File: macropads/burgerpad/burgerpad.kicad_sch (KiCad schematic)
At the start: 1 part, among them U1 RP2040-ZERO

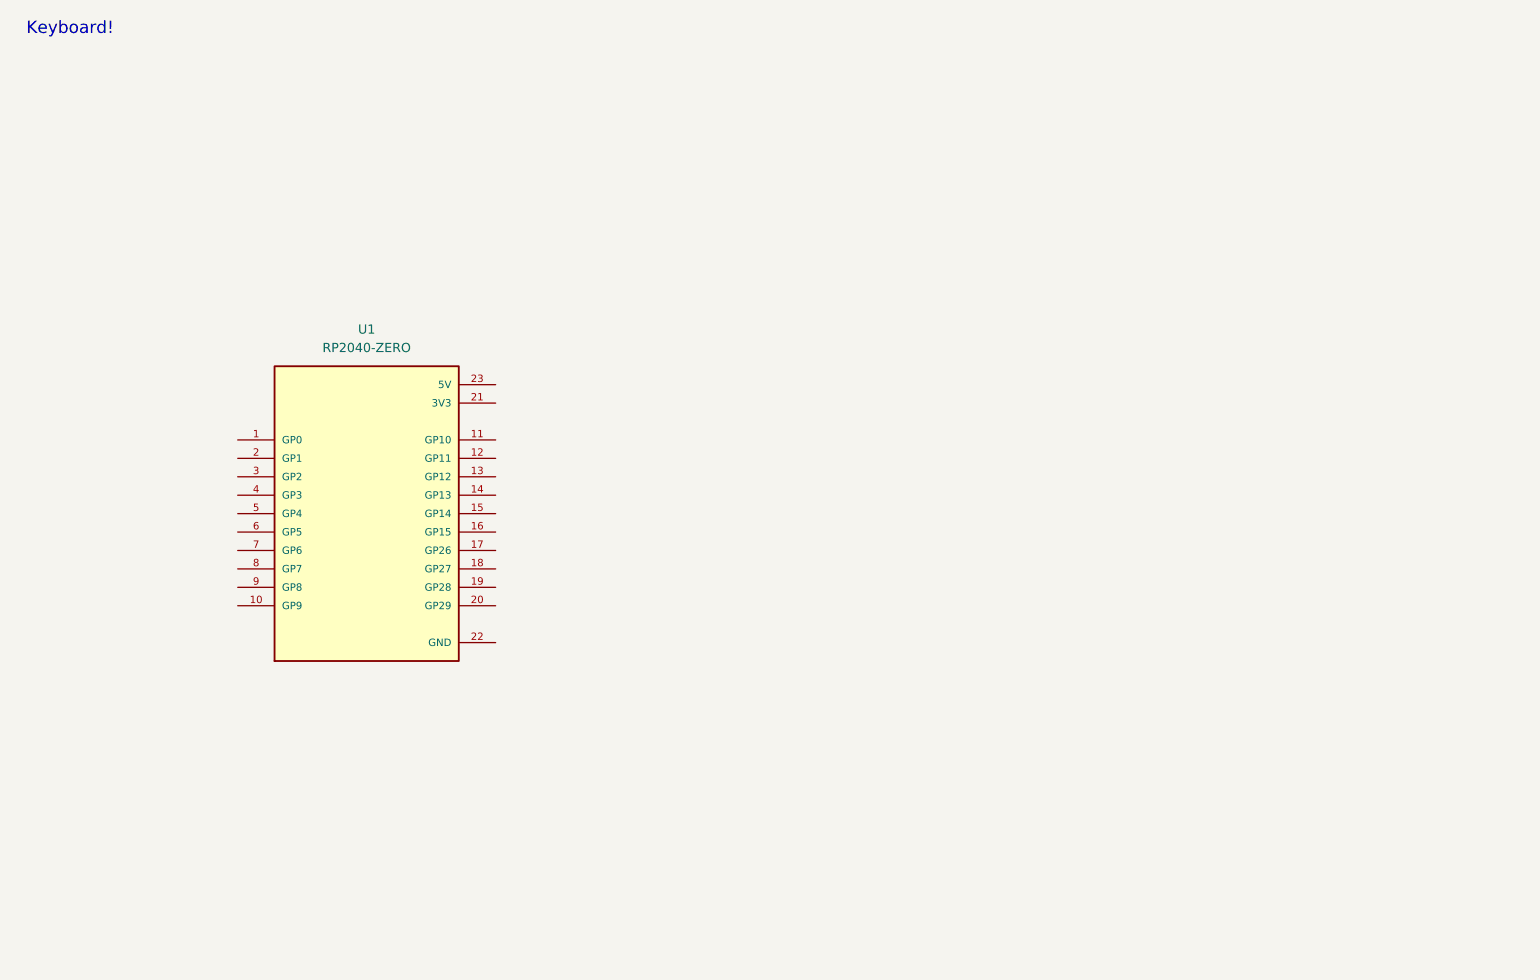
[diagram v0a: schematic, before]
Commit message: Made schematic and did PCB layouts
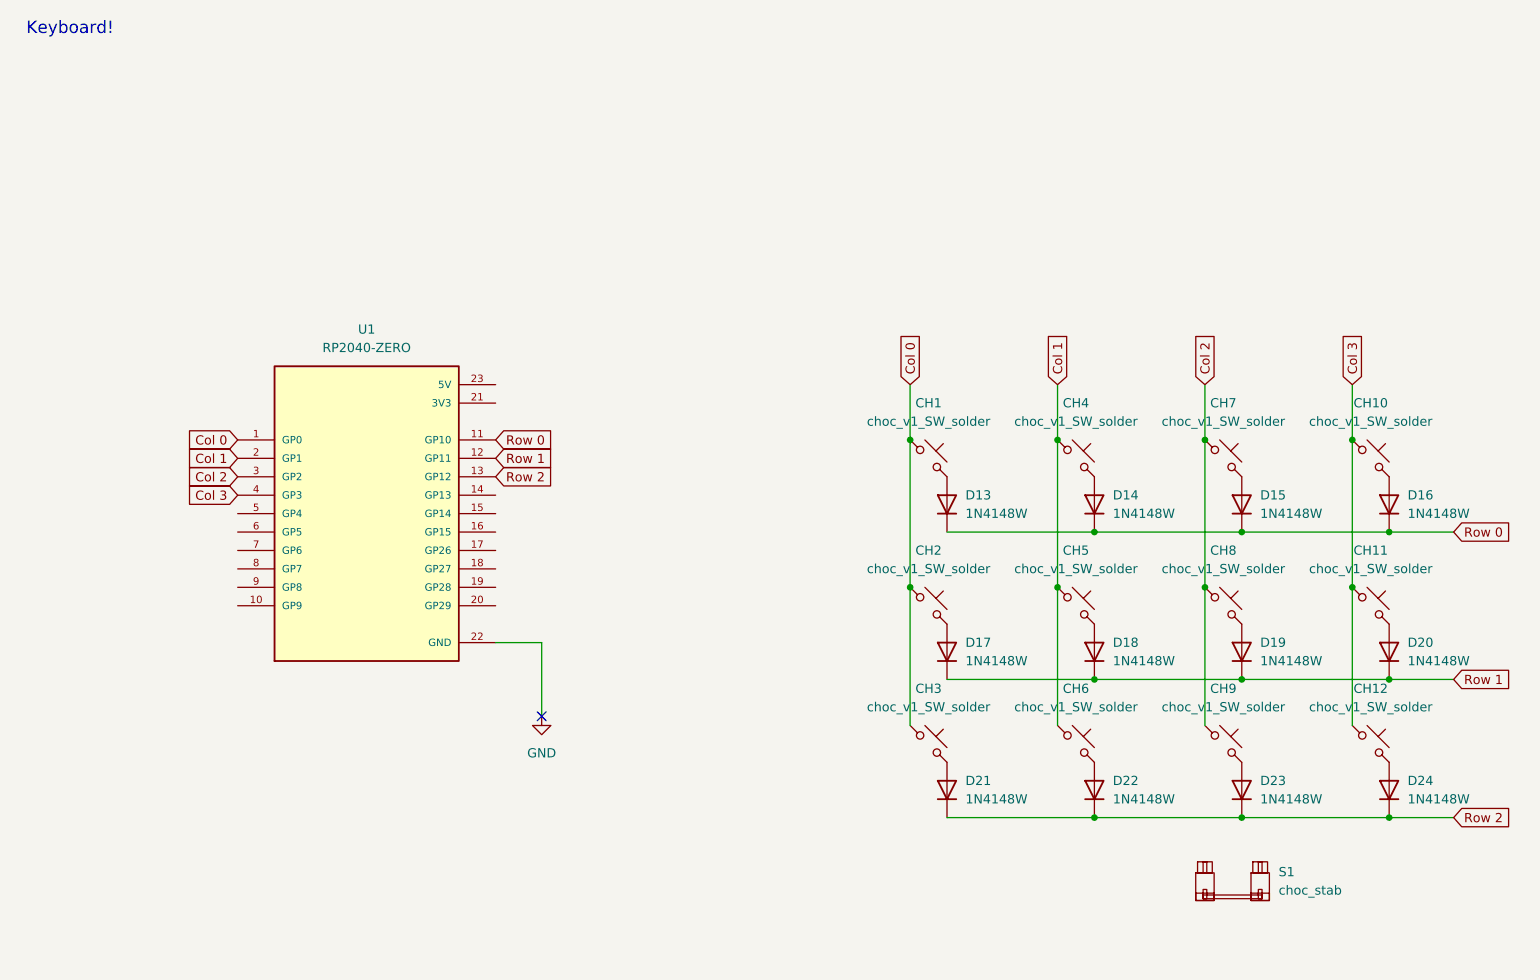
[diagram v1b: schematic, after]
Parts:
- added CH1, CH10, CH11, CH12, CH2, CH3, CH4, CH5, CH6, CH7, CH8, CH9: choc_v1_SW_solder, PCM_marbastlib-choc:SW_choc_v1_1u, symbol PCM_marbastlib-choc:choc_v1_SW_solder
- added D13, D14, D15, D16, D17, D18, D19, D20, D21, D22, D23, D24: 1N4148W, Diode_SMD:D_SOD-123, symbol Diode:1N4148W
- added S1: choc_stab, PCM_marbastlib-xp-choc:STAB_choc_2u, symbol PCM_marbastlib-choc:choc_stab
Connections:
- net Col 0: now reaches U1.1 (GP0)
- net Col 0: now also CH1.1, CH2.1, CH3.1
- net Row 0: now reaches U1.11 (GP10)
- net Row 0: now also D13.1 (K), D14.1 (K), D15.1 (K), D16.1 (K)
- net Row 1: now reaches U1.12 (GP11)
- net Row 1: now also D17.1 (K), D18.1 (K), D19.1 (K), D20.1 (K)
- net Row 2: now reaches U1.13 (GP12)
- net Row 2: now also D21.1 (K), D22.1 (K), D23.1 (K), D24.1 (K)
- net Col 1: now reaches U1.2 (GP1)
- net Col 1: now also CH4.1, CH5.1, CH6.1
- net GND: now reaches U1.22 (GND)
- net Col 2: now reaches U1.3 (GP2)
- net Col 2: now also CH7.1, CH8.1, CH9.1
- net Col 3: now reaches U1.4 (GP3)
- net Col 3: now also CH10.1, CH11.1, CH12.1
- new net: CH4.2, D14.2 (A)
- new net: CH12.2, D24.2 (A)
- new net: CH6.2, D22.2 (A)
- new net: CH1.2, D13.2 (A)
- new net: CH7.2, D15.2 (A)
- new net: CH11.2, D20.2 (A)
- new net: CH10.2, D16.2 (A)
- new net: CH8.2, D19.2 (A)
- new net: CH3.2, D21.2 (A)
- new net: CH5.2, D18.2 (A)
- new net: CH2.2, D17.2 (A)
- new net: CH9.2, D23.2 (A)
- no-connect marks 0 -> 1

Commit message: Updated schematic and PCB to match new layout
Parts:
- removed S1: choc_stab, PCM_marbastlib-xp-choc:STAB_choc_2u, symbol PCM_marbastlib-choc:choc_stab
- added CH13: choc_v1_SW_solder, PCM_marbastlib-choc:SW_choc_v1_1u, symbol PCM_marbastlib-choc:choc_v1_SW_solder
- added D25: 1N4148W, Diode_SMD:D_SOD-123, symbol Diode:1N4148W
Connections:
- net Col 3: now also CH13.1
- net Row 3: now reaches U1.14 (GP13)
- net Row 3: now also D25.1 (K)
- new net: CH13.2, D25.2 (A)
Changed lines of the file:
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@@
 	)
 	(junction
+		(at 199.39 111.76)
+		(diameter 0)
+		(color 0 0 0 0)
+	)
+	(junction
 		(at 158.75 72.39)
 		(diameter 0)
@@
 	(wire
 		(pts
+			(xy 199.39 111.76) (xy 199.39 130.81)
+		)
+		(stroke
+			(width 0)
+			(type default)
+		)
+	)
+	(wire
+		(pts
 			(xy 199.39 64.77) (xy 199.39 72.39)
 		)
@@
 	(wire
 		(pts
+			(xy 204.47 143.51) (xy 213.36 143.51)
+		)
+		(stroke
+			(width 0)
+			(type default)
+		)
+	)
+	(wire
+		(pts
 			(xy 143.51 105.41) (xy 163.83 105.41)
 		)
@@
 		)
 	)
+	(global_label "Row 3"
+		(shape input)
+		(at 81.28 80.01 0)
+		(fields_autoplaced yes)
+		(effects
+			(font
+				(size 1.27 1.27)
+			)
+			(justify left)
+		)
+		(property "Intersheetrefs" "${INTERSHEET_REFS}"
+			(at 90.1918 80.01 0)
+			(hide yes)
+			(show_name no)
+			(do_not_autoplace no)
+			(effects
+				(font
+					(size 1.27 1.27)
+				)
+				(justify left)
+			)
+		)
+	)
 	(global_label "Col 1"
 		(shape input)
@@
 		)
 	)
+	(global_label "Row 3"
+		(shape input)
+		(at 213.36 143.51 0)
+		(fields_autoplaced yes)
+		(effects
+			(font
+				(size 1.27 1.27)
+			)
+			(justify left)
+		)
+		(property "Intersheetrefs" "${INTERSHEET_REFS}"
+			(at 222.2718 143.51 0)
+			(hide yes)
+			(show_name no)
+			(do_not_autoplace no)
+			(effects
+				(font
+					(size 1.27 1.27)
+				)
+				(justify left)
+			)
+		)
+	)
 	(global_label "Row 0"
 		(shape input)
@@
 	(symbol
 		(lib_id "Diode:1N4148W")
+		(at 204.47 139.7 90)
+		(unit 1)
+		(body_style 1)
+		(exclude_from_sim no)
+		(in_bom yes)
+		(on_board yes)
+		(in_pos_files yes)
+		(dnp no)
+		(fields_autoplaced yes)
+		(property "Reference" "D25"
+			(at 207.01 138.4299 90)
+			(show_name no)
+			(do_not_autoplace no)
+			(effects
+				(font
+					(size 1.27 1.27)
+				)
+				(justify right)
+			)
+		)
+		(property "Value" "1N4148W"
+			(at 207.01 140.9699 90)
+			(show_name no)
+			(do_not_autoplace no)
+			(effects
+				(font
+					(size 1.27 1.27)
+				)
+				(justify right)
+			)
+		)
+		(property "Footprint" "Diode_SMD:D_SOD-123"
+			(at 208.915 139.7 0)
+			(hide yes)
+			(show_name no)
+			(do_not_autoplace no)
+			(effects
+				(font
+					(size 1.27 1.27)
+				)
+			)
+		)
+		(property "Datasheet" "https://www.vishay.com/docs/85748/1n4148w.pdf"
+			(at 204.47 139.7 0)
+			(hide yes)
+			(show_name no)
+			(do_not_autoplace no)
+			(effects
+				(font
+					(size 1.27 1.27)
+				)
+			)
+		)
+		(property "Description" "75V 0.15A Fast Switching Diode, SOD-123"
+			(at 204.47 139.7 0)
+			(hide yes)
+			(show_name no)
+			(do_not_autoplace no)
+			(effects
+				(font
+					(size 1.27 1.27)
+				)
+			)
+		)
+		(property "Sim.Device" "D"
+			(at 204.47 139.7 0)
+			(hide yes)
+			(show_name no)
+			(do_not_autoplace no)
+			(effects
+				(font
+					(size 1.27 1.27)
+				)
+			)
+		)
+		(property "Sim.Pins" "1=K 2=A"
+			(at 204.47 139.7 0)
+			(hide yes)
+			(show_name no)
+			(do_not_autoplace no)
+			(effects
+				(font
+					(size 1.27 1.27)
+				)
+			)
+		)
+		(pin "2"
+		)
+		(pin "1"
+		)
+		(instances
+			(project "burgerpad"
+				(path "/614136c8-a77d-46c5-b91b-b3698493ea5b"
+					(reference "D25")
+					(unit 1)
+				)
+			)
+		)
+	)
+	(symbol
+		(lib_id "Diode:1N4148W")
 		(at 143.51 81.28 90)
 		(unit 1)
@@
 	)
 	(symbol
-		(lib_id "PCM_marbastlib-choc:choc_stab")
-		(at 182.88 133.35 0)
-		(unit 1)
-		(body_style 1)
-		(exclude_from_sim no)
-		(in_bom yes)
-		(on_board yes)
-		(in_pos_files yes)
-		(dnp no)
-		(fields_autoplaced yes)
-		(property "Reference" "S1"
-			(at 189.23 131.9529 0)
-			(show_name no)
-			(do_not_autoplace no)
-			(effects
-				(font
-					(size 1.27 1.27)
-				)
-				(justify left)
-			)
-		)
-		(property "Value" "choc_stab"
-			(at 189.23 134.4929 0)
-			(show_name no)
-			(do_not_autoplace no)
-			(effects
-				(font
-					(size 1.27 1.27)
-				)
-				(justify left)
-			)
-		)
-		(property "Footprint" "PCM_marbastlib-xp-choc:STAB_choc_2u"
-			(at 182.88 133.35 0)
-			(hide yes)
-			(show_name no)
-			(do_not_autoplace no)
-			(effects
-				(font
-					(size 1.27 1.27)
-				)
-			)
-		)
-		(property "Datasheet" ""
-			(at 182.88 133.35 0)
-			(hide yes)
-			(show_name no)
-			(do_not_autoplace no)
-			(effects
-				(font
-					(size 1.27 1.27)
-				)
-			)
-		)
-		(property "Description" "Kailh Choc-style stabilizer"
-			(at 182.88 133.35 0)
-			(hide yes)
-			(show_name no)
-			(do_not_autoplace no)
-			(effects
-				(font
-					(size 1.27 1.27)
-				)
-			)
-		)
-		(instances
-			(project "burgerpad"
-				(path "/614136c8-a77d-46c5-b91b-b3698493ea5b"
-					(reference "S1")
-					(unit 1)
-				)
-			)
-		)
-	)
-	(symbol
 		(lib_id "PCM_marbastlib-choc:choc_v1_SW_solder")
 		(at 181.61 114.3 0)
@@
 					(unit 1)
 				)
+			)
+		)
+	)
+	(symbol
+		(lib_id "PCM_marbastlib-choc:choc_v1_SW_solder")
+		(at 201.93 133.35 0)
+		(unit 1)
+		(body_style 1)
+		(exclude_from_sim no)
+		(in_bom yes)
+		(on_board yes)
+		(in_pos_files yes)
+		(dnp no)
+		(fields_autoplaced yes)
+		(property "Reference" "CH13"
+			(at 201.93 125.73 0)
+			(show_name no)
+			(do_not_autoplace no)
+			(effects
+				(font
+					(size 1.27 1.27)
+				)
+			)
+		)
+		(property "Value" "choc_v1_SW_solder"
+			(at 201.93 128.27 0)
+			(show_name no)
+			(do_not_autoplace no)
+			(effects
+				(font
+					(size 1.27 1.27)
+				)
+			)
+		)
+		(property "Footprint" "PCM_marbastlib-choc:SW_choc_v1_1u"
+			(at 201.93 133.35 0)
+			(hide yes)
+			(show_name no)
+			(do_not_autoplace no)
+			(effects
+				(font
+					(size 1.27 1.27)
+				)
+			)
+		)
+		(property "Datasheet" ""
+			(at 201.93 133.35 0)
+			(hide yes)
+			(show_name no)
+			(do_not_autoplace no)
+			(effects
+				(font
+					(size 1.27 1.27)
+				)
+			)
+		)
+		(property "Description" "Push button switch, normally open, two pins, 45° tilted"
+			(at 201.93 133.35 0)
+			(hide yes)
+			(show_name no)
+			(do_not_autoplace no)
+			(effects
+				(font
+					(size 1.27 1.27)
+				)
+			)
+		)
+		(pin "1"
+		)
+		(pin "2"
+		)
+		(instances
+			(project "burgerpad"
+				(path "/614136c8-a77d-46c5-b91b-b3698493ea5b"
+					(reference "CH13")
+					(unit 1)
+				)
